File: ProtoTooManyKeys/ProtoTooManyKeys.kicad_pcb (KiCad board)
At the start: 2 copper layers, 125.5 x 53.8 mm, 74 parts, among them J1 54104-3031_Oled, J2 AVR-ISP-6, SW1 SW_Push, U1 PRTR5V0U2X, U2 AT90USB1286-AU, U3 PCA9306TDCURQ1, U4 AZ1117CH-3.3TRG1, Y1 16MHz

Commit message: Routing finished
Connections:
- U2 pad 33: Net-(U2-Pad33) -> ROW1
- U2 pad 34: Net-(U2-Pad34) -> ROW0
- U2 pad 49: ROW1 -> Net-(U2-Pad49)
- U2 pad 50: ROW0 -> Net-(U2-Pad50)
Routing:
- net SW15: track 0.00 -> 168.5 mm, vias 0 -> 6
- net CS18: track 0.00 -> 162.8 mm, vias 0 -> 6
- net CS17: track 0.00 -> 137.7 mm, vias 0 -> 4
- net ROW1: track 40.0 -> 166.0 mm, vias 0 -> 4
- net SW14: track 0.00 -> 106.5 mm, vias 0 -> 8
- net ROW0: track 39.0 -> 145.0 mm, vias 0 -> 4
- net SW3: track 22.2 -> 127.1 mm, vias 0 -> 4
- net COL01: track 20.2 -> 124.3 mm, vias 0 -> 3
- net SW13: track 0.00 -> 102.9 mm, vias 0 -> 8
- net COL00: track 20.2 -> 106.4 mm, vias 0 -> 3
- net CS2: track 0.00 -> 83.1 mm, vias 0 -> 4
- net SW2: track 25.5 -> 91.4 mm, vias 2 -> 5
- net CS1: track 0.00 -> 62.9 mm, vias 0 -> 4
- net SW1: track 22.2 -> 78.2 mm, vias 2 -> 6
- net GND: track 93.0 -> 104.1 mm
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
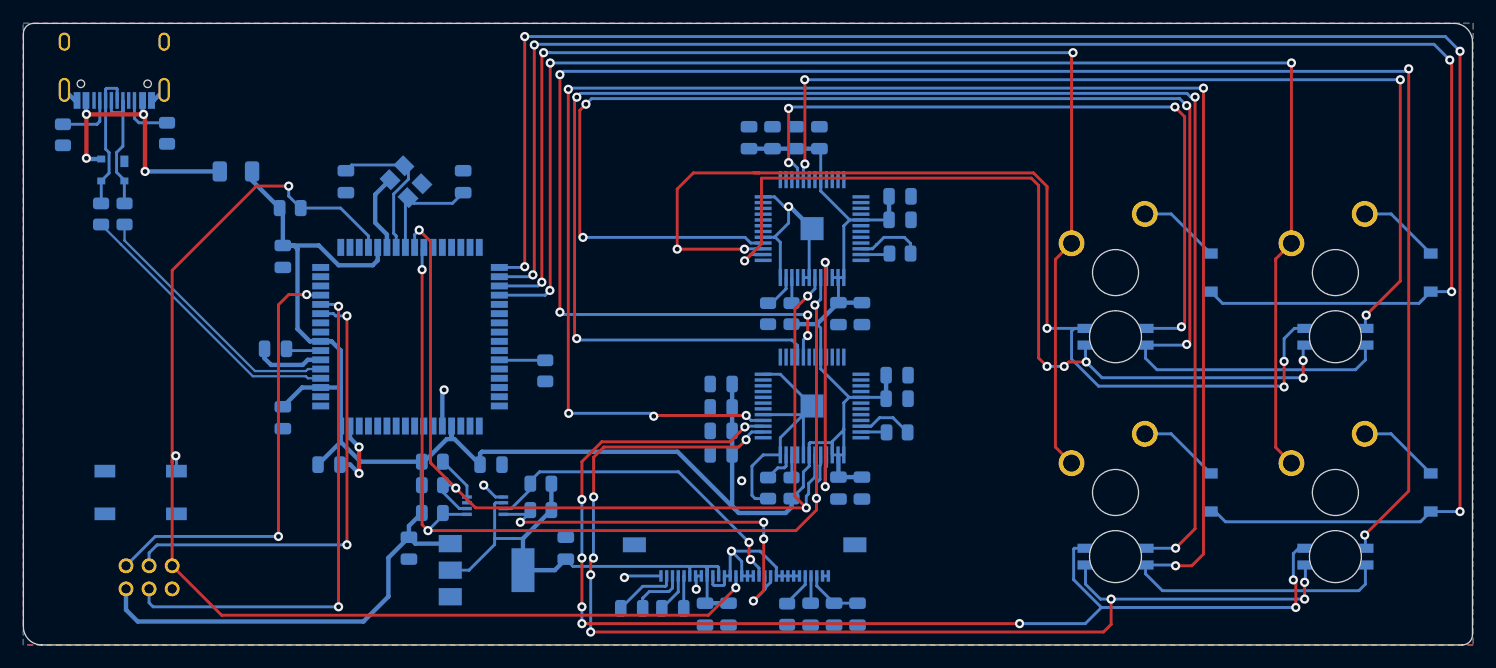
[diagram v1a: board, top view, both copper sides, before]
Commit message: Final touches on Proto and added a missing capacitor
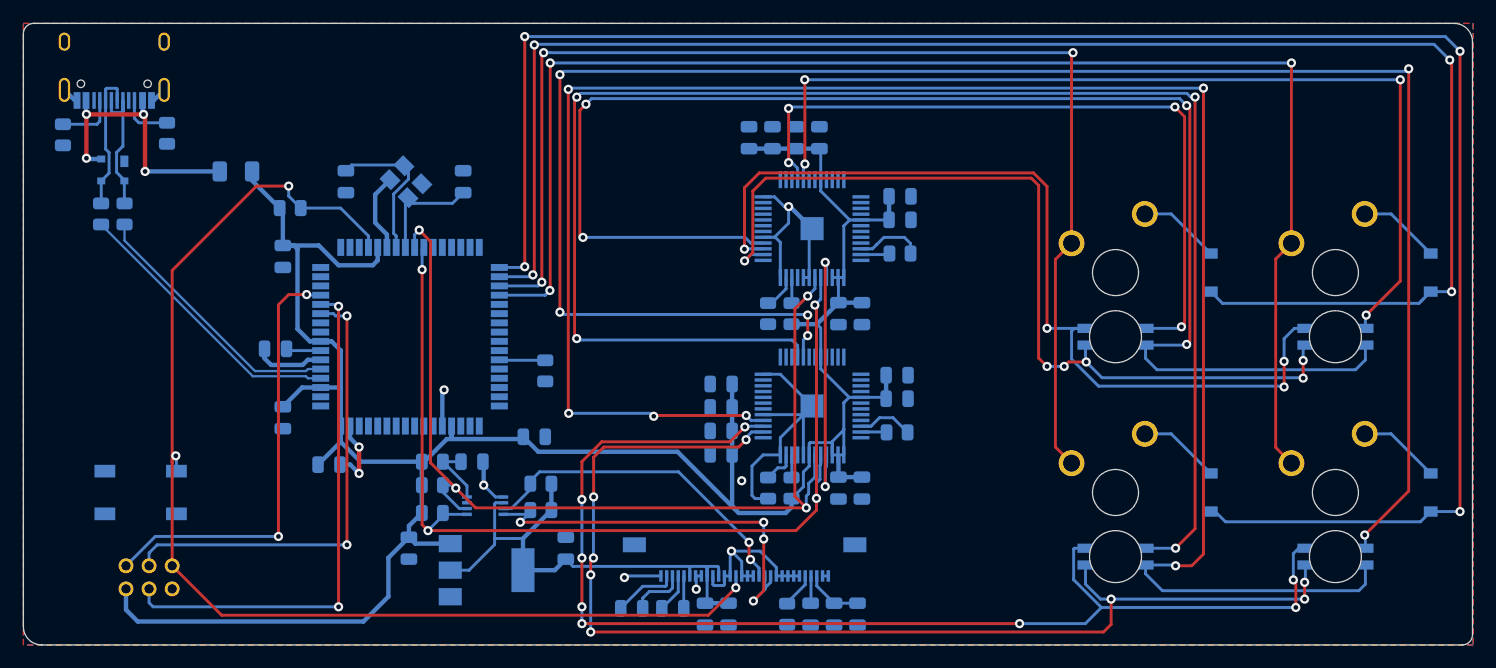
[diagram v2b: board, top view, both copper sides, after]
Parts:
- added C33: 100pF, Capacitor_SMD:C_0805_2012Metric, B.Cu at (376.0, 403.7)
- moved C11 4.46 mm to (381.4, 401.6)
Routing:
- net SW2: track 91.4 -> 79.3 mm, vias 5 -> 4
- net GND: track 104.1 -> 106.2 mm
- net Net-(C33-Pad2): track 4.42 -> 5.99 mm
- net +5V: track 216.1 -> 214.8 mm
- net SW1: track 78.2 -> 77.0 mm

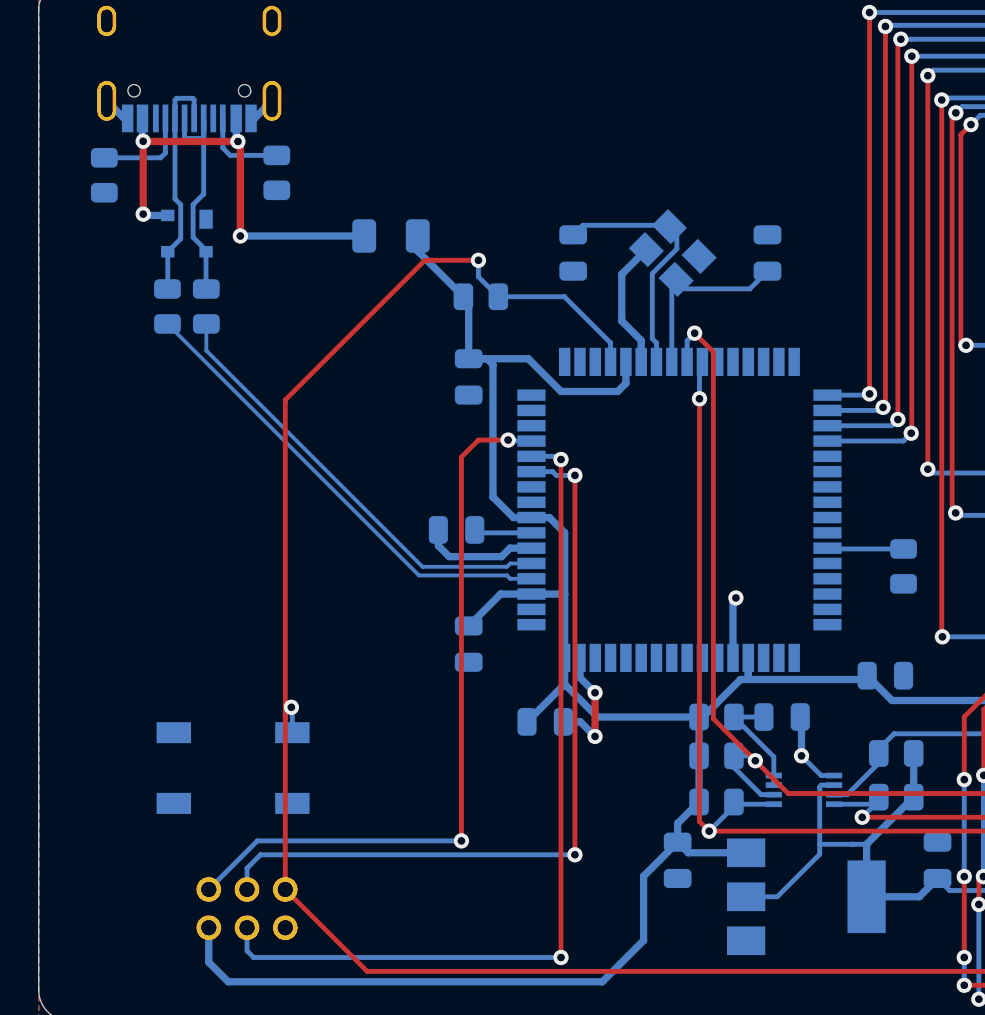
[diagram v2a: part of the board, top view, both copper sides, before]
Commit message: routing fixes, new gerber files
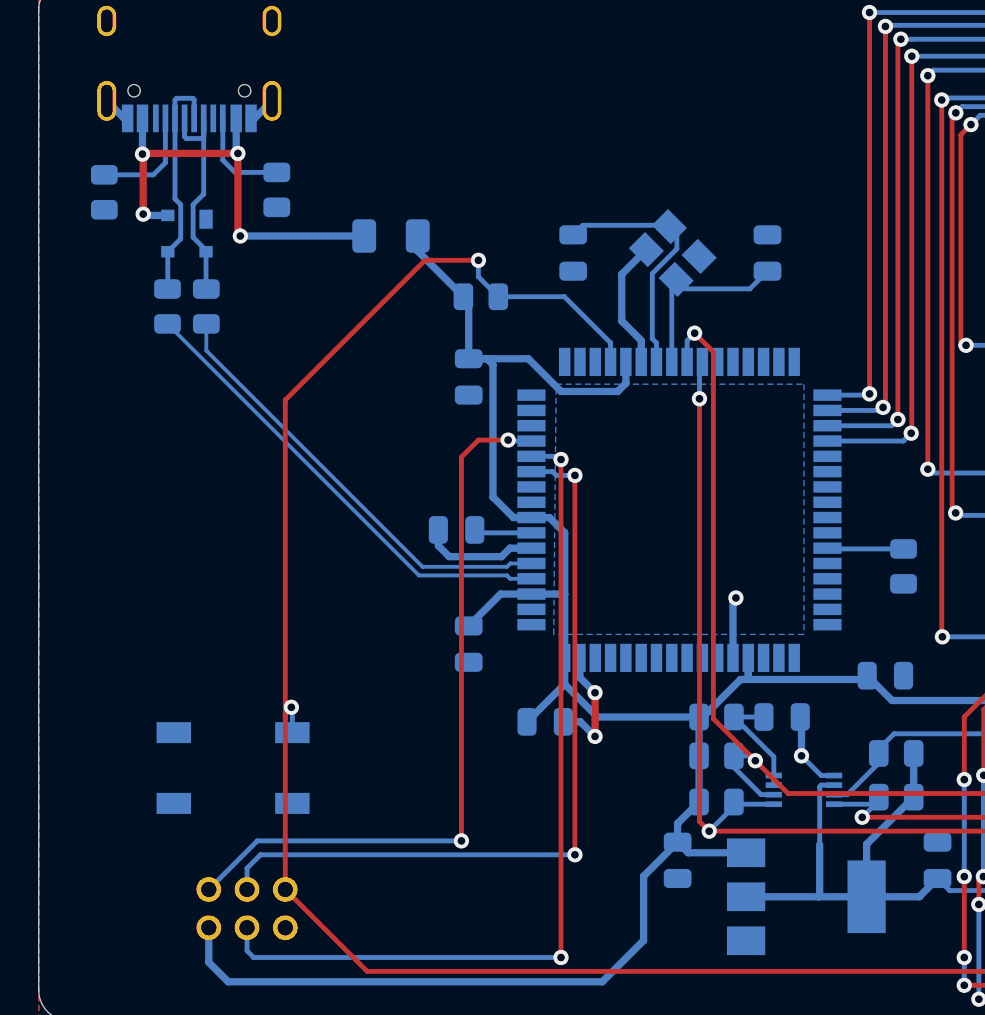
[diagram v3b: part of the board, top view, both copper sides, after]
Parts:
- moved R4 0.89 mm to (340.6, 376.3)
- moved R7 0.89 mm to (349.6, 376.2)
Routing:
- net +3V3: track 45.3 -> 48.2 mm
- net Net-(R7-Pad2): track 4.53 -> 5.27 mm
- net Net-(R4-Pad2): track 5.11 -> 5.77 mm
